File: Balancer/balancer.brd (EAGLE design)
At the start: 139.7 x 325.1 mm, 322 parts, among them Q1 BSS123W, Q10A SIR882DP-T1-GE3, Q10B SIS468DN-T1-GE3, Q11A SIR882DP-T1-GE3, Q11B SIS468DN-T1-GE3, Q12A SIR882DP-T1-GE3, Q12B SIS468DN-T1-GE3, Q1A8 SIR882DP-T1-GE3, Q1B8 SIS468DN-T1-GE3, Q2 BSS123W, Q3A SIR882DP-T1-GE3, Q3B SIS468DN-T1-GE3, Q4 MMBT3906LT1G, Q4A SIR882DP-T1-GE3, Q4B SIS468DN-T1-GE3, Q5 FDN5618P, Q5A SIR882DP-T1-GE3, Q5B SIS468DN-T1-GE3, Q6 CMPT3904E_TR_PBFREE, Q6A SIR882DP-T1-GE3, Q6B SIS468DN-T1-GE3, Q9A SIR882DP-T1-GE3, Q9B SIS468DN-T1-GE3, T10 750312504, T11 750312504, T12 750312504, T3 750312504, T4 750312504, T5 750312504, T6 750312504, T8 750312504, T9 750312504, U1 LTC3300ILXE-1PBF, U2 LTC3300ILXE-1PBF

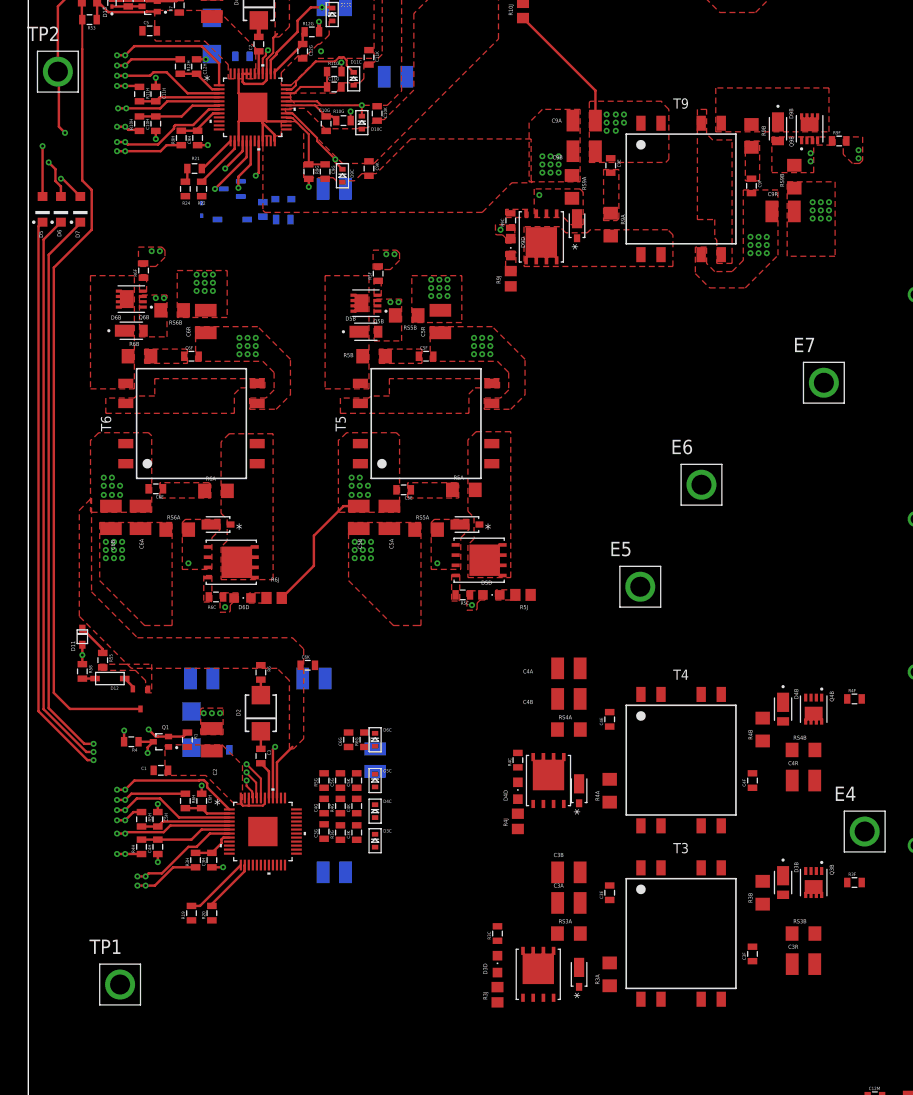
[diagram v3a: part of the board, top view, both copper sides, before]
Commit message: done most of L1 wiring
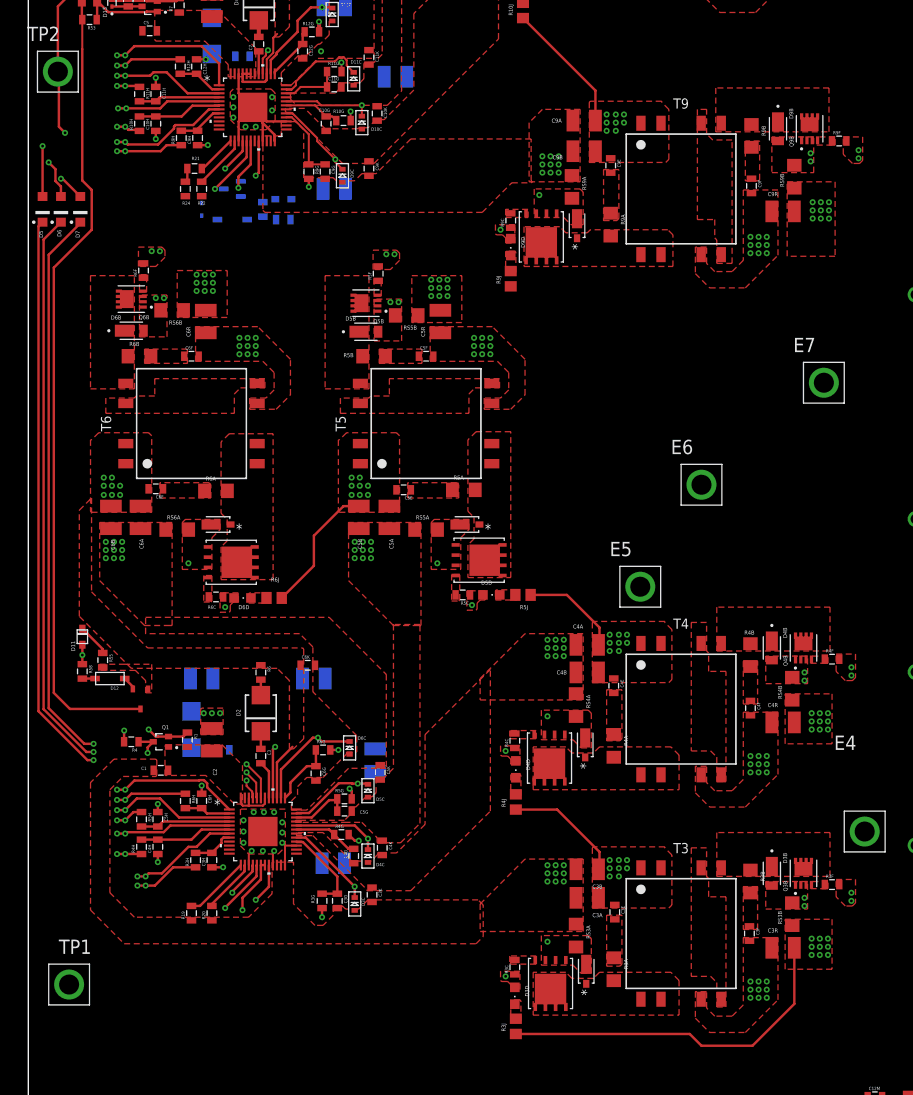
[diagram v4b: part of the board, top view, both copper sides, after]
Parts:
- moved R4B 9.40 mm to (89.9, 174.4), turned to 270 degrees
- moved C4F 9.02 mm to (89.9, 167.8), turned to 270 degrees
- moved R3G 8.81 mm to (36.6, 143.8), turned to 270 degrees
- moved C3G 8.79 mm to (38.5, 143.8), turned to 270 degrees
- moved D3C 8.27 mm to (40.6, 143.4)
- moved C3K 7.98 mm to (42.8, 144.5), turned to 270 degrees
- moved D4B 7.75 mm to (92.6, 175.3)
- moved RS4B 7.75 mm to (95.1, 170.2), turned to 90 degrees
- moved Q4B 7.73 mm to (96.5, 175.3), turned to 90 degrees
- moved C4R 7.67 mm to (94.0, 166.0)
- moved C4G 7.23 mm to (40.5, 149.4), turned to 270 degrees
- moved TP1 6.35 mm to (5.08, 133.3)
- moved T4 6.35 mm to (81.3, 167.6)
- moved C4K 6.10 mm to (44.1, 150.4), turned to 270 degrees
- moved C6G 5.84 mm to (35.8, 159.6), turned to 270 degrees
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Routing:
- net V-: track 4.42 -> 56.9 mm, vias 25 -> 64
- net C3: track 0.00 -> 14.8 mm, vias 0 -> 17
- net G6P: track 0.00 -> 13.9 mm, vias 1 -> 2
- net C4: track 0.00 -> 12.5 mm, vias 9 -> 17
- net G3P: track 0.00 -> 11.1 mm, vias 0 -> 2
- net G4P: track 0.00 -> 10.9 mm, vias 0 -> 2
- net I3P: track 0.00 -> 10.9 mm
- net G5P: track 0.00 -> 10.5 mm, vias 1 -> 2
- net I6P: track 0.00 -> 8.25 mm
- net I4P: track 0.00 -> 8.12 mm
- net I5P: track 0.00 -> 7.56 mm
- net SDIO: track 0.00 -> 7.05 mm, vias 0 -> 1
- net SCKI: track 0.00 -> 6.98 mm, vias 0 -> 1
- net WDTA: track 5.40 -> 10.4 mm, vias 1 -> 2
- net CSBI: track 0.00 -> 4.50 mm, vias 0 -> 1
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- added copper zone on layer 1, net C3
- added copper zone on layer 1, net G3P
- added copper zone on layer 1, net G3S
- added copper zone on layer 1, net G4P
- added copper zone on layer 1, net G4S
- added copper zone on layer 1, net N$10
- added copper zone on layer 1, net N$11
- added copper zone on layer 1, net N$110
- added copper zone on layer 1, net N$12
- added copper zone on layer 1, net N$15
- added copper zone on layer 1, net N$16
- added copper zone on layer 1, net N$17
- added copper zone on layer 1, net N$19
- added copper zone on layer 1, net N$20
- added copper zone on layer 1, net N$24
- added copper zone on layer 1, net N$27
- added copper zone on layer 1, net N$29
- added copper zone on layer 1, net N$31
- added copper zone on layer 1, net N$32
- added copper zone on layer 1, net N$33
- added copper zone on layer 1, net N$35
- added copper zone on layer 1, net N$36
- added copper zone on layer 1, net N$8
- added copper zone on layer 1, net N$87
- added copper zone on layer 1, net N$9

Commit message: done majority of L1 wiring
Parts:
- removed C10M, C11M, C12M, C13M, C3M, C4M, C5M, C6M, C9M: 10nF, Ilya_Teach:0805
- removed R10K, R11K, R12K, R13K, R3K, R4K, R5K, R6K, R8K, R9K: 100, rcl:R0805
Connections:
- removed net C0_F: C13M.1, C3M.1, CN2.9, R13K.2
- removed net C10_F: C10M.1, C11M.2, CN2.6, R10K.2
- removed net C11_F: C11M.1, C12M.2, CN2.7, R11K.2
- removed net C12_F: C12M.1, CN2.8, R12K.2
- removed net C3_F: C3M.2, C4M.2, CN2.1, R3K.2
- removed net C4_F: C4M.1, C5M.2, CN2.2, R4K.2
- removed net C5_F: C5M.1, C6M.1, CN2.3, R5K.2
- removed net C6_F: C6M.2, CN2.4, R6K.2
- removed net C9_F: C10M.2, C9M.1, CN2.5, R9K.2
- removed net N$98: C9M.2, R8K.2
- net C10: now also CN2.6; no longer R10K.1
- net C11: now also CN2.7; no longer R11K.1
- net C12: now also CN2.8; no longer R12K.1
- net C3: now also CN2.1; no longer R3K.1
- net C4: now also CN2.2; no longer R4K.1
- net C5: now also CN2.3; no longer R5K.1
- net C6: now also CN2.4; no longer R6K.1, R8K.1
- net C9: now also CN2.5; no longer R9K.1
- net V-: now also CN2.9; no longer C13M.2, R13K.1

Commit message: modified position of E8 and E15
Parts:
- moved CN2 122.7 mm to (8.89, 120.7)
- moved F13 121.0 mm to (147.3, 105.4), turned to 90 degrees
- moved JP1 112.8 mm to (8.89, 86.4)
- moved E15 111.3 mm to (151.1, 198.1)
- moved C10F 109.1 mm to (114.3, 160.5)
- moved C10R 109.1 mm to (118.0, 157.5)
- moved C11A 109.1 mm to (65.3, 173.4)
- moved C11B 109.1 mm to (61.7, 173.4)
- moved C12K 109.1 mm to (55.9, 154.4)
- moved C15 109.1 mm to (44.5, 153.7)
- moved C24 109.1 mm to (55.9, 157.5)
- moved E11 109.1 mm to (130.8, 153.7)
- moved R10C 109.1 mm to (84.5, 155.2)
- moved T11 109.1 mm to (69.8, 185.4)
- moved T12 109.1 mm to (39.4, 185.4)
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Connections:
- net BAT+: no longer E15.1, E8.1
- net BOT6_TS: now also E8.1
- net C10: now also CN2.7; no longer CN2.6
- net C11: now also CN2.8; no longer CN2.7
- net C12: now also CN2.9; no longer CN2.8
- net C3: now also CN2.2; no longer CN2.1
- net C4: now also CN2.3; no longer CN2.2
- net C5: now also CN2.4; no longer CN2.3
- net C6: now also CN2.5; no longer CN2.4
- net C9: now also CN2.6; no longer CN2.5
- net TOP6_TS: now also E15.1
- net V-: now also CN2.1; no longer CN2.9
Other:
- board size 139.7 x 325.1 mm -> 170 x 230 mm

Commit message: L1 mostly done, L2 done
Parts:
- moved JP1 158.5 mm to (151.1, 16.5)
- moved CN2 157.3 mm to (149.9, 50.8)
- moved E8 94.9 mm to (110.5, 104.1)
- moved F14 85.0 mm to (130.8, 124.5), flipped to the top, turned to 270 degrees
- moved E15 76.8 mm to (108.0, 134.6)
- moved E11 41.6 mm to (95.2, 132.1)
- moved CN1 34.5 mm to (146.1, 110.5)
- moved C13 33.5 mm to (114.3, 83.8), turned to 270 degrees
- moved E1 33.4 mm to (114.3, 15.2)
- moved E13 33.0 mm to (99.1, 180.3)
- moved D12E 29.2 mm to (118.1, 190.5)
- moved D11E 27.9 mm to (118.1, 170.2)
- moved D10E 25.6 mm to (119.4, 147.3)
- moved D9E 25.5 mm to (116.8, 128.3)
- moved D5E 24.4 mm to (120.7, 66.0)
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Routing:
- net C12: track 11.4 -> 156.2 mm
- net SDIO: track 7.05 -> 139.8 mm
- net C11: track 15.2 -> 144.1 mm
- net SCKI: track 6.98 -> 132.1 mm
- net CSBI: track 4.50 -> 128.3 mm
- net C10: track 17.8 -> 131.2 mm
- net BAT+: track 0.00 -> 108.0 mm
- net BOT6_TS: track 1.40 -> 99.1 mm
- net C9: track 16.5 -> 110.4 mm
- net N$30: track 0.00 -> 87.1 mm
- net N$28: track 0.00 -> 69.5 mm
- net WDTA: track 10.4 -> 75.4 mm
- net N$14: track 0.00 -> 61.4 mm
- net C6: track 32.2 -> 87.9 mm
- net N$26: track 0.00 -> 53.2 mm
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
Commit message: Finished L3 wiring
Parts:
- moved C16 2.54 mm to (52.1, 141.0)
- moved D3 1.27 mm to (36.8, 135.9)
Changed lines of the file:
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@@
 <grid distance="50" unitdist="mil" unit="mil" style="lines" multiple="1" display="no" altdistance="5" altunitdist="mil" altunit="mil"/>
 <layers>
-<layer number="1" name="Top" color="4" fill="1" visible="yes" active="yes"/>
-<layer number="2" name="Route2" color="16" fill="1" visible="yes" active="yes"/>
+<layer number="1" name="Top" color="4" fill="1" visible="no" active="yes"/>
+<layer number="2" name="Route2" color="16" fill="1" visible="no" active="yes"/>
 <layer number="3" name="Route3" color="17" fill="1" visible="no" active="no"/>
 <layer number="4" name="Route4" color="18" fill="1" visible="no" active="no"/>
@@
 <layer number="13" name="Route13" color="21" fill="1" visible="no" active="no"/>
 <layer number="14" name="Route14" color="22" fill="1" visible="no" active="no"/>
-<layer number="15" name="Route15" color="13" fill="1" visible="no" active="yes"/>
-<layer number="16" name="Bottom" color="1" fill="1" visible="yes" active="yes"/>
+<layer number="15" name="Route15" color="13" fill="1" visible="yes" active="yes"/>
+<layer number="16" name="Bottom" color="1" fill="1" visible="no" active="yes"/>
 <layer number="17" name="Pads" color="2" fill="1" visible="yes" active="yes"/>
 <layer number="18" name="Vias" color="2" fill="1" visible="yes" active="yes"/>
@@
 <attribute name="VALUE" x="37.465" y="140.335" size="1.27" layer="28" rot="MR0"/>
 </element>
-<element name="C16" library="rcl" library_urn="urn:adsk.eagle:library:334" package="C1210" package3d_urn="urn:adsk.eagle:package:23619/2" value="4.7uF" x="52.07" y="138.43" smashed="yes" rot="MR0">
-<attribute name="NAME" x="53.975" y="140.335" size="1.27" layer="26" rot="MR0"/>
-<attribute name="POPULARITY" value="6" x="-148.59" y="-34.29" size="1.778" layer="28" rot="MR0" display="off"/>
-<attribute name="SPICEPREFIX" value="C" x="-148.59" y="-34.29" size="1.778" layer="28" rot="MR0" display="off"/>
-<attribute name="VALUE" x="53.975" y="135.255" size="1.27" layer="28" rot="MR0"/>
+<element name="C16" library="rcl" library_urn="urn:adsk.eagle:library:334" package="C1210" package3d_urn="urn:adsk.eagle:package:23619/2" value="4.7uF" x="52.07" y="140.97" smashed="yes" rot="MR0">
+<attribute name="NAME" x="53.975" y="142.875" size="1.27" layer="26" rot="MR0"/>
+<attribute name="POPULARITY" value="6" x="-148.59" y="-31.75" size="1.778" layer="28" rot="MR0" display="off"/>
+<attribute name="SPICEPREFIX" value="C" x="-148.59" y="-31.75" size="1.778" layer="28" rot="MR0" display="off"/>
+<attribute name="VALUE" x="53.975" y="137.795" size="1.27" layer="28" rot="MR0"/>
 </element>
 <element name="C17" library="rcl" library_urn="urn:adsk.eagle:library:334" package="C1210" package3d_urn="urn:adsk.eagle:package:23619/2" value="4.7uF" x="59.69" y="129.54" smashed="yes" rot="MR0">
@@
 <attribute name="VALUE" x="46.136" y="48.252" size="0.8128" layer="27" rot="R90"/>
 </element>
-<element name="D3" library="DO-214AA" package="WE-TVSP_DO-214AA_UNIDIRECTIONAL" value="WE-TVSP_DO-214AA_600W_UNI" x="36.83" y="134.62" smashed="yes" rot="MR90">
-<attribute name="AVAILABILITY" value="In Stock" x="-128.27" y="274.32" size="1.778" layer="28" rot="MR90" display="off"/>
-<attribute name="CHECK_PRICES" value="https://www.snapeda.com/parts/824520141/W%25C3%25BCrth+Elektronik+Midcom/view-part/?ref=eda" x="-128.27" y="274.32" size="1.778" layer="28" rot="MR90" display="off"/>
-<attribute name="DESCRIPTION" value="                                                      23.2V Clamp 25.9A Ipp Tvs Diode Surface Mount DO-214AA                                              " x="-128.27" y="274.32" size="1.778" layer="28" rot="MR90" display="off"/>
-<attribute name="MF" value="Würth Elektronik" x="-128.27" y="274.32" size="1.778" layer="28" rot="MR90" display="off"/>
-<attribute name="MP" value="824520141" x="-128.27" y="274.32" size="1.778" layer="28" rot="MR90" display="off"/>
-<attribute name="NAME" x="39.37" y="134.68" size="0.8128" layer="26" rot="MR90" align="bottom-center"/>
-<attribute name="PACKAGE" value="DO-214 Würth Elektronik" x="-128.27" y="274.32" size="1.778" layer="28" rot="MR90" display="off"/>
-<attribute name="PRICE" value="None" x="-128.27" y="274.32" size="1.778" layer="28" rot="MR90" display="off"/>
-<attribute name="SNAPEDA_LINK" value="https://www.snapeda.com/parts/824520141/W%25C3%25BCrth+Elektronik+Midcom/view-part/?ref=snap" x="-128.27" y="274.32" size="1.778" layer="28" rot="MR90" display="off"/>
-<attribute name="VALUE" x="33.62" y="132.58" size="0.8128" layer="28" rot="MR90"/>
+<element name="D3" library="DO-214AA" package="WE-TVSP_DO-214AA_UNIDIRECTIONAL" value="WE-TVSP_DO-214AA_600W_UNI" x="36.83" y="135.89" smashed="yes" rot="MR90">
+<attribute name="AVAILABILITY" value="In Stock" x="-128.27" y="275.59" size="1.778" layer="28" rot="MR90" display="off"/>
+<attribute name="CHECK_PRICES" value="https://www.snapeda.com/parts/824520141/W%25C3%25BCrth+Elektronik+Midcom/view-part/?ref=eda" x="-128.27" y="275.59" size="1.778" layer="28" rot="MR90" display="off"/>
+<attribute name="DESCRIPTION" value="                                                      23.2V Clamp 25.9A Ipp Tvs Diode Surface Mount DO-214AA                                              " x="-128.27" y="275.59" size="1.778" layer="28" rot="MR90" display="off"/>
+<attribute name="MF" value="Würth Elektronik" x="-128.27" y="275.59" size="1.778" layer="28" rot="MR90" display="off"/>
+<attribute name="MP" value="824520141" x="-128.27" y="275.59" size="1.778" layer="28" rot="MR90" display="off"/>
+<attribute name="NAME" x="39.37" y="135.95" size="0.8128" layer="26" rot="MR90" align="bottom-center"/>
+<attribute name="PACKAGE" value="DO-214 Würth Elektronik" x="-128.27" y="275.59" size="1.778" layer="28" rot="MR90" display="off"/>
+<attribute name="PRICE" value="None" x="-128.27" y="275.59" size="1.778" layer="28" rot="MR90" display="off"/>
+<attribute name="SNAPEDA_LINK" value="https://www.snapeda.com/parts/824520141/W%25C3%25BCrth+Elektronik+Midcom/view-part/?ref=snap" x="-128.27" y="275.59" size="1.778" layer="28" rot="MR90" display="off"/>
+<attribute name="VALUE" x="33.62" y="133.85" size="0.8128" layer="28" rot="MR90"/>
 </element>
 <element name="D3A" library="balancer" package="SDO_POWERDI123_DIO" value="DFLS260Q-7" x="83.439" y="18.161" smashed="yes" rot="R90">
@@
 </polygon>
 <polygon width="0.1524" layer="15" isolate="0.3048" thermals="no">
-<vertex x="15.24" y="111.76"/>
-<vertex x="130.81" y="111.76"/>
+<vertex x="15.24" y="109.855"/>
+<vertex x="130.81" y="109.855"/>
 <vertex x="130.81" y="207.01"/>
 <vertex x="15.24" y="207.01"/>
@@
 </polygon>
 <polygon width="0.1524" layer="15" isolate="0.3048" thermals="no">
-<vertex x="15.24" y="109.22"/>
-<vertex x="130.81" y="109.22"/>
+<vertex x="15.24" y="106.172"/>
+<vertex x="130.81" y="106.172"/>
 <vertex x="130.81" y="8.89"/>
 <vertex x="15.24" y="8.89"/>
@@
 <wire x1="120.3" y1="144.458" x2="127" y2="138.8872" width="0" layer="19" extent="16-16"/>
 <wire x1="118.46" y1="144.458" x2="120.3" y2="144.458" width="0" layer="19" extent="16-16"/>
-<wire x1="50.67" y1="138.43" x2="46.0883" y2="125.48" width="0" layer="19" extent="1-16"/>
+<wire x1="50.67" y1="140.97" x2="46.0883" y2="125.48" width="0" layer="19" extent="1-16"/>
 </signal>
 <signal name="N$91">
@@
 <wire x1="127.7493" y1="179.0722125" x2="148.5342" y2="158.2873125" width="0.3048" layer="2"/>
 <wire x1="148.5342" y1="158.2873125" x2="148.5342" y2="64.080625" width="0.3048" layer="2"/>
-<wire x1="51.816" y1="136.487" x2="53.47" y2="138.43" width="0" layer="19" extent="1-16"/>
+<wire x1="51.816" y1="136.487" x2="53.47" y2="140.97" width="0" layer="19" extent="1-16"/>
 <wire x1="39.74" y1="132.08" x2="46.0883" y2="128.48" width="0" layer="19" extent="1-16"/>
 <wire x1="119.03" y1="187.638" x2="127" y2="182.0672" width="0" layer="19" extent="16-16"/>
@@
 <wire x1="43.16" y1="131.79686875" x2="43.5514" y2="132.18826875" width="0.254" layer="1"/>
 <wire x1="43.815" y1="132.842" x2="41.54" y2="132.08" width="0" layer="19" extent="16-16"/>
-<wire x1="36.83" y1="132.37" x2="41.54" y2="132.08" width="0" layer="19" extent="16-16"/>
+<wire x1="36.83" y1="133.64" x2="41.54" y2="132.08" width="0" layer="19" extent="16-16"/>
 </signal>
 <signal name="N$152">
@@
 <contactref element="D4" pad="1"/>
 <wire x1="42.672" y1="134.504" x2="42.672" y2="136.561" width="0.508" layer="1"/>
-<wire x1="36.83" y1="136.87" x2="42.672" y2="136.561" width="0" layer="19" extent="1-16"/>
+<wire x1="36.83" y1="138.14" x2="42.672" y2="136.561" width="0" layer="19" extent="1-16"/>
 </signal>
 <signal name="N$53">
